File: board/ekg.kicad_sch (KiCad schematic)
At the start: 34 parts

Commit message: updated schematic after review
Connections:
- net +3V3: now also R?.1
- net MUX_{SW} renamed GPIO1
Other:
- moved on the sheet: R?
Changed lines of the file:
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@@
     (stroke (width 0) (type default) (color 0 0 0 0))
   )
-  (wire (pts (xy 91.44 118.11) (xy 91.44 117.475))
+  (wire (pts (xy 91.44 116.84) (xy 91.44 118.11))
     (stroke (width 0) (type default) (color 0 0 0 0))
   )
@@
     (effects (font (size 1.27 1.27)) (justify left bottom))
   )
-  (label "MUX_{SW}" (at 121.92 99.06 180)
-    (effects (font (size 1.27 1.27)) (justify right bottom))
-  )
   (label "SCK" (at 113.4056 123.19 0)
     (effects (font (size 1.27 1.27)) (justify left bottom))
@@
   )
   (hierarchical_label "GPIO2" (shape bidirectional) (at 121.92 101.6 180)
+    (effects (font (size 1.27 1.27)) (justify right))
+  )
+  (hierarchical_label "GPIO1" (shape bidirectional) (at 121.92 99.06 180)
     (effects (font (size 1.27 1.27)) (justify right))
   )
@@
     (pin "1")
     (pin "2")
+  )
+  (symbol (lib_id "power:+3V3") (at 91.44 111.76 0) (unit 1)
+    (in_bom yes) (on_board yes) (fields_autoplaced)
+    (property "Reference" "#PWR?" (id 0) (at 91.44 115.57 0)
+      (effects (font (size 1.27 1.27)) hide)
+    )
+    (property "Value" "+3V3" (id 1) (at 93.98 110.4899 0)
+      (effects (font (size 1.27 1.27)) (justify left))
+    )
+    (property "Footprint" "" (id 2) (at 91.44 111.76 0)
+      (effects (font (size 1.27 1.27)) hide)
+    )
+    (property "Datasheet" "" (id 3) (at 91.44 111.76 0)
+      (effects (font (size 1.27 1.27)) hide)
+    )
+    (pin "1")
   )
   (symbol (lib_id "Device:C_Small") (at 100.33 48.26 0) (unit 1)
@@
     (pin "2")
   )
-  (symbol (lib_id "Device:R_Small") (at 91.44 114.935 0) (unit 1)
-    (in_bom yes) (on_board yes) (fields_autoplaced)
-    (property "Reference" "R?" (id 0) (at 93.98 113.6649 0)
-      (effects (font (size 1.27 1.27)) (justify left))
-    )
-    (property "Value" "~" (id 1) (at 93.98 116.2049 0)
-      (effects (font (size 1.27 1.27)) (justify left))
-    )
-    (property "Footprint" "" (id 2) (at 91.44 114.935 0)
-      (effects (font (size 1.27 1.27)) hide)
-    )
-    (property "Datasheet" "~" (id 3) (at 91.44 114.935 0)
-      (effects (font (size 1.27 1.27)) hide)
-    )
+  (symbol (lib_id "Device:R_Small") (at 91.44 114.3 0) (unit 1)
+    (in_bom yes) (on_board yes) (fields_autoplaced)
+    (property "Reference" "R?" (id 0) (at 93.98 113.0299 0)
+      (effects (font (size 1.27 1.27)) (justify left))
+    )
+    (property "Value" "~" (id 1) (at 93.98 115.5699 0)
+      (effects (font (size 1.27 1.27)) (justify left))
+    )
+    (property "Footprint" "" (id 2) (at 91.44 114.3 0)
+      (effects (font (size 1.27 1.27)) hide)
+    )
+    (property "Datasheet" "~" (id 3) (at 91.44 114.3 0)
+      (effects (font (size 1.27 1.27)) hide)
+    )

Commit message: updated schematic
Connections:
- net CS renamed ~{CS}
- net SCK renamed CLK
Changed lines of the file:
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@@
   (no_connect (at 121.92 135.89))
   (no_connect (at 121.92 133.35))
-  (bus_entry (at 110.49 123.19) (size -2.54 2.54)
-    (stroke (width 0) (type default) (color 0 0 0 0))
-  )
-  (bus_entry (at 110.49 113.03) (size -2.54 2.54)
-    (stroke (width 0) (type default) (color 0 0 0 0))
-  )
-  (bus_entry (at 110.49 110.49) (size -2.54 2.54)
-    (stroke (width 0) (type default) (color 0 0 0 0))
-  )
-  (bus_entry (at 110.49 115.57) (size -2.54 2.54)
-    (stroke (width 0) (type default) (color 0 0 0 0))
-  )
   (wire (pts (xy 172.72 69.85) (xy 190.5 69.85))
     (stroke (width 0) (type default) (color 0 0 0 0))
@@
     (stroke (width 0) (type default) (color 0 0 0 0))
   )
-  (wire (pts (xy 110.49 115.57) (xy 121.92 115.57))
-    (stroke (width 0) (type default) (color 0 0 0 0))
-  )
   (wire (pts (xy 158.75 62.23) (xy 167.64 62.23))
     (stroke (width 0) (type default) (color 0 0 0 0))
@@
     (stroke (width 0) (type default) (color 0 0 0 0))
   )
-  (bus (pts (xy 97.79 127) (xy 107.95 127))
-    (stroke (width 0) (type default) (color 0 0 0 0))
-  )
   (wire (pts (xy 115.57 73.66) (xy 121.92 73.66))
     (stroke (width 0) (type default) (color 0 0 0 0))
@@
     (stroke (width 0) (type default) (color 0 0 0 0))
   )
-  (wire (pts (xy 110.49 113.03) (xy 121.92 113.03))
-    (stroke (width 0) (type default) (color 0 0 0 0))
-  )
   (wire (pts (xy 82.55 36.83) (xy 121.92 36.83))
     (stroke (width 0) (type default) (color 0 0 0 0))
@@
     (stroke (width 0) (type default) (color 0 0 0 0))
   )
-  (bus (pts (xy 107.95 118.11) (xy 107.95 125.73))
-    (stroke (width 0) (type default) (color 0 0 0 0))
-  )
   (wire (pts (xy 97.79 155.575) (xy 102.87 155.575))
     (stroke (width 0) (type default) (color 0 0 0 0))
@@
     (stroke (width 0) (type default) (color 0 0 0 0))
   )
-  (bus (pts (xy 107.95 110.49) (xy 107.95 113.03))
-    (stroke (width 0) (type default) (color 0 0 0 0))
-  )
   (wire (pts (xy 119.38 118.11) (xy 119.38 119.38))
     (stroke (width 0) (type default) (color 0 0 0 0))
@@
     (stroke (width 0) (type default) (color 0 0 0 0))
   )
-  (bus (pts (xy 107.95 115.57) (xy 107.95 118.11))
-    (stroke (width 0) (type default) (color 0 0 0 0))
-  )
   (wire (pts (xy 148.59 90.17) (xy 158.75 90.17))
     (stroke (width 0) (type default) (color 0 0 0 0))
@@
     (stroke (width 0) (type default) (color 0 0 0 0))
   )
-  (wire (pts (xy 110.49 123.19) (xy 121.92 123.19))
-    (stroke (width 0) (type default) (color 0 0 0 0))
-  )
   (wire (pts (xy 91.44 116.84) (xy 91.44 118.11))
     (stroke (width 0) (type default) (color 0 0 0 0))
@@
     (stroke (width 0) (type default) (color 0 0 0 0))
   )
-  (bus (pts (xy 107.95 113.03) (xy 107.95 115.57))
-    (stroke (width 0) (type default) (color 0 0 0 0))
-  )
   (wire (pts (xy 119.38 85.09) (xy 121.92 85.09))
     (stroke (width 0) (type default) (color 0 0 0 0))
@@
     (stroke (width 0) (type default) (color 0 0 0 0))
   )
-  (wire (pts (xy 110.49 110.49) (xy 121.92 110.49))
-    (stroke (width 0) (type default) (color 0 0 0 0))
-  )
   (wire (pts (xy 104.14 149.86) (xy 104.14 175.26))
     (stroke (width 0) (type default) (color 0 0 0 0))
@@
   )
   (wire (pts (xy 148.59 92.71) (xy 149.86 92.71))
-    (stroke (width 0) (type default) (color 0 0 0 0))
-  )
-  (bus (pts (xy 107.95 125.73) (xy 107.95 127))
     (stroke (width 0) (type default) (color 0 0 0 0))
   )
@@
     (effects (font (size 1.27 1.27)) (justify left bottom))
   )
-  (label "MOSI" (at 113.03 113.03 0)
-    (effects (font (size 1.27 1.27)) (justify left bottom))
-  )
-  (label "MISO" (at 113.03 115.57 0)
-    (effects (font (size 1.27 1.27)) (justify left bottom))
-  )
-  (label "CS" (at 113.03 110.49 0)
-    (effects (font (size 1.27 1.27)) (justify left bottom))
-  )
-  (label "SCK" (at 113.4056 123.19 0)
-    (effects (font (size 1.27 1.27)) (justify left bottom))
-  )
-  (hierarchical_label "SPI" (shape bidirectional) (at 97.79 127 180)
+  (hierarchical_label "~{CS}" (shape input) (at 121.92 110.49 180)
     (effects (font (size 1.27 1.27)) (justify right))
   )
@@
     (effects (font (size 1.27 1.27)) (justify right))
   )
+  (hierarchical_label "CLK" (shape input) (at 121.92 123.19 180)
+    (effects (font (size 1.27 1.27)) (justify right))
+  )
   (hierarchical_label "GPIO4" (shape bidirectional) (at 121.92 106.68 180)
     (effects (font (size 1.27 1.27)) (justify right))
   )
+  (hierarchical_label "MISO" (shape output) (at 121.92 115.57 180)
+    (effects (font (size 1.27 1.27)) (justify right))
+  )
   (hierarchical_label "~{DRDY}" (shape output) (at 86.36 118.11 180)
     (effects (font (size 1.27 1.27)) (justify right))
   )
+  (hierarchical_label "MOSI" (shape input) (at 121.92 113.03 180)
+    (effects (font (size 1.27 1.27)) (justify right))
+  )

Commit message: ERC run
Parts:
- added R8: 10k, symbol Device:R_Small
- gave numbers to parts that had none: 34
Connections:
- net DGND is gone; now on net AVSS: C10.2, C13.2, U2.33 (DGND), U2.49 (DGND), U2.51 (DGND)
- net DVDD is gone; now on net +3V3: C10.1, C13.1, U2.48 (DVDD), U2.50 (DVDD)
- net +3V3: no longer U2.52 (CLKSEL)
- net AVSS: now also R8.1
- net MCLK: now reaches U2.37 (CLK)
- new net: R8.2, U2.52 (CLKSEL)
- no-connect marks 4 -> 2

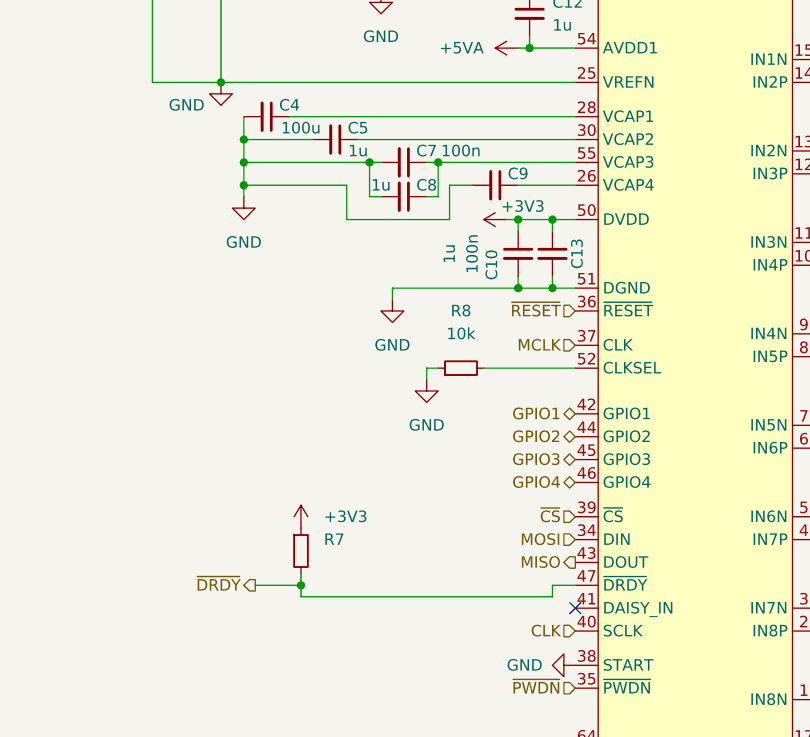
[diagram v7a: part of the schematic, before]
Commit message: added footprints to symbols and started layout
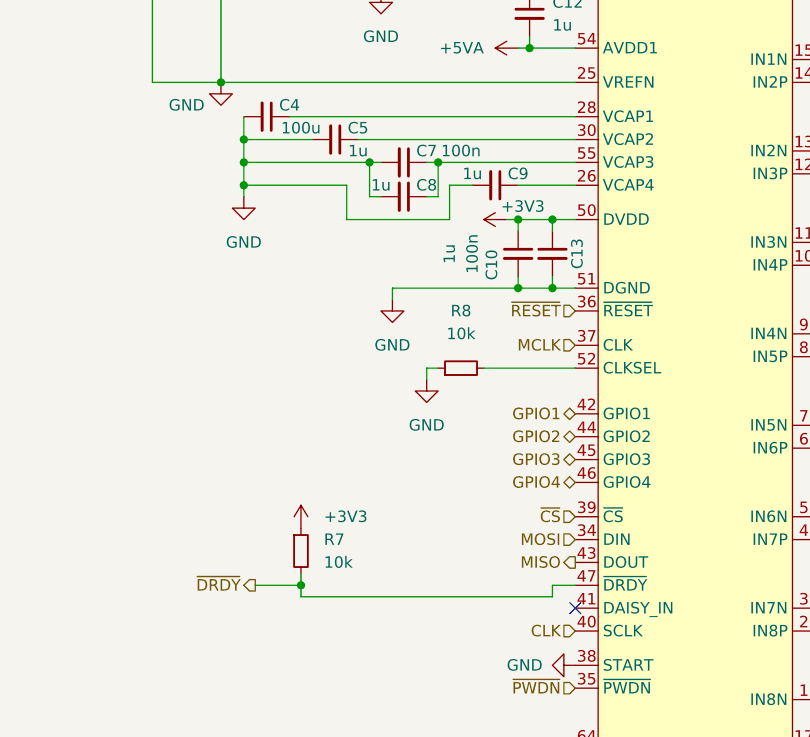
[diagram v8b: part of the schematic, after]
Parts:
- C1, C14, C15, C16, C17: footprint (none) -> Capacitor_SMD:C_0603_1608Metric_Pad1.08x0.95mm_HandSolder
- C10, C11, C12, C2, C5, C6, C8: footprint (none) -> Capacitor_SMD:C_0603_1608Metric
- C13, C3, C7: footprint (none) -> Capacitor_SMD:C_0402_1005Metric
- C4: footprint (none) -> Capacitor_SMD:C_1206_3216Metric
- C9: value ~ -> 1u; footprint (none) -> Capacitor_SMD:C_0603_1608Metric
- J2: footprint (none) -> Connector_PinHeader_2.54mm:PinHeader_1x05_P2.54mm_Vertical
- J3: footprint (none) -> Connector_PinHeader_2.54mm:PinHeader_1x02_P2.54mm_Vertical
- JP1, JP2, JP3: footprint (none) -> Connector_PinHeader_2.54mm:PinHeader_1x03_P2.54mm_Vertical
- R10, R11, R12, R13, R14, R15, R16, R5, R6, R9: footprint (none) -> Resistor_SMD:R_0603_1608Metric_Pad0.98x0.95mm_HandSolder
- R7: value ~ -> 10k; footprint (none) -> Resistor_SMD:R_0402_1005Metric
- R8: footprint (none) -> Resistor_SMD:R_0402_1005Metric
- U2: footprint (none) -> Package_QFP:TQFP-64_10x10mm_P0.5mm
